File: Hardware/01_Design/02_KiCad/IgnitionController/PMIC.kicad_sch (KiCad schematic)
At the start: 0 parts

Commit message: PMIC HW implementation
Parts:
- added 8.2K1: R, symbol Device:R
- added C1: 100nF, symbol Device:C
- added C13, C3, C4, C5: 100n, Capacitor_SMD:C_0805_2012Metric_Pad1.18x1.45mm_HandSolder, symbol Device:C
- added C2: 100n, symbol Device:C
- added Q1: SS8050, Package_TO_SOT_SMD:SOT-563, symbol Transistor_BJT:SS8050
- added Q2, Q3: DMP6050SSD, Package_SO:SOIC-8_3.9x4.9mm_P1.27mm, symbol Transistor_FET:DMP6050SSD
- added R15, R5, R6, R7: 475R, Resistor_SMD:R_0805_2012Metric_Pad1.20x1.40mm_HandSolder, symbol Device:R
- added R16, R17, R18, R19: 0R, Resistor_SMD:R_0805_2012Metric_Pad1.20x1.40mm_HandSolder, symbol Device:R
- added R20, R21, R22: 8.2K, Resistor_SMD:R_0805_2012Metric_Pad1.20x1.40mm_HandSolder, symbol Device:R
- added R24, R26, R30, R32: 30K, Resistor_SMD:R_0805_2012Metric_Pad1.20x1.40mm_HandSolder, symbol Device:R
- added R25, R27, R29, R31, R33, R35, R36, R37, R38: 10K, Resistor_SMD:R_0805_2012Metric_Pad1.20x1.40mm_HandSolder, symbol Device:R
- added R28: 10k, Resistor_SMD:R_0805_2012Metric_Pad1.20x1.40mm_HandSolder, symbol Device:R
- added R34: 43k, Resistor_SMD:R_0805_2012Metric_Pad1.20x1.40mm_HandSolder, symbol Device:R
- added TP1: PMIC_CLK, TestPoint:TestPoint_Plated_Hole_D3.0mm, symbol Connector:TestPoint
- added TP2: SPI_CS, TestPoint:TestPoint_Plated_Hole_D3.0mm, symbol Connector:TestPoint
- added TP3: SPI_MOSI, TestPoint:TestPoint_Plated_Hole_D3.0mm, symbol Connector:TestPoint
- added TP4: SPI_MISO, TestPoint:TestPoint_Plated_Hole_D3.0mm, symbol Connector:TestPoint
- added TP5: SPI_SCK, TestPoint:TestPoint_Plated_Hole_D3.0mm, symbol Connector:TestPoint
- added TP6: KL30_ADC, TestPoint:TestPoint_Plated_Hole_D3.0mm, symbol Connector:TestPoint
- added TP7: KL15_ADC, TestPoint:TestPoint_Plated_Hole_D3.0mm, symbol Connector:TestPoint
- added TP8: VSEN_ADC, TestPoint:TestPoint_Plated_Hole_D3.0mm, symbol Connector:TestPoint
- added TP9: VMCU_ADC, TestPoint:TestPoint_Plated_Hole_D3.0mm, symbol Connector:TestPoint
- added U1: ATmega328PB-A, Package_QFP:TQFP-32_7x7mm_P0.8mm, symbol MCU_Microchip_ATmega:ATmega328PB-A
- added U10, U11: TLV2372, Package_SO:SOIC-8_5.3x6.2mm_P1.27mm, symbol Amplifier_Operational:TLV2372
- added U2, U5, U6, U7: 4N35, Package_DIP:DIP-6_W7.62mm, symbol Isolator:4N35
- added U8: TXS0104EPW, Package_SO:TSSOP-14_4.4x5mm_P0.65mm, symbol Logic_LevelTranslator:TXS0104EPW
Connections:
- new net: C3.1, R22.2, TP8.1, U11.1, U11.2 (-)
- new net: C2.1, R21.2, TP7.1, U10.6 (-), U10.7
- new net: Q3.2 (G1), U6.4
- new net: Q1.2 (E), R33.1, U8.8 (OE)
- new net: R18.1, U6.6
- new net: R30.2, R31.1, U11.5 (+)
- new net: 8.2K1.2, C4.1, TP9.1, U11.6 (-), U11.7
- new net: Q2.4 (G2), U5.4
- new net: C13.2, U1.20 (AREF)
- new net: R20.1, U1.23 (PC0)
- new net: C1.1, R20.2, TP6.1, U10.1, U10.2 (-)
- new net: R16.1, U2.6
- new net: TP2.1, U1.14 (PB2), U8.13 (B1)
- new net: Q3.4 (G2), U7.4
- new net: R7.2, U6.1
- new net: R28.2, TP1.1, U1.12 (PB0)
- new net: TP3.1, U1.15 (PB3), U8.12 (B2)
- new net: TP4.1, U1.16 (PB4), U8.11 (B3)
- new net: TP5.1, U1.17 (PB5), U8.10 (B4)
- new net: R21.1, U1.24 (PC1)
- new net: R22.1, U1.25 (PC2)
- new net: 8.2K1.1, U1.26 (PC3)
- new net: R5.1, U1.27 (PC4)
- new net: R6.1, U1.28 (PC5)
- new net: R7.1, U1.29 (~{RESET}/PC6)
- new net: R15.1, U1.30 (PD0)
- new net: Q2.2 (G1), U2.4
- new net: R19.1, U7.6
- new net: R29.1, R32.2, U11.3 (+)
- new net: R6.2, U5.1
- new net: R17.1, U5.6
- new net: R24.2, R25.1, U10.3 (+)
- new net: Q1.1 (B), R34.1
- new net: R15.2, U7.1
- new net: R5.2, U2.1
- new net: R26.2, R27.1, U10.5 (+)
- new net +BATT: Q2.1 (S1), Q2.3 (S2), R24.1, U2.5, U5.5
- new net GND: C1.2, C13.1, C2.2, C3.2, C4.2, C5.1, R16.2, R17.2, R18.2, R19.2, R25.2, R27.2, R28.1, R29.2, R31.2, R33.2, R35.2, R36.2, R37.2, R38.2, U1.21 (GND), U1.5 (GND), U10.4 (V-), U11.4 (V-), U2.2, U5.2, U6.2, U7.2, U8.7 (GND)
- new net KL15: R26.1
- new net KL15_OUT: Q2.5 (D2), Q2.6 (D2), R37.1
- new net KL30_OUT: Q2.7 (D1), Q2.8 (D1), R38.1
- new net MCU_SPI_CS: U8.2 (A1)
- new net MCU_SPI_MISO: U8.4 (A3)
- new net MCU_SPI_MOSI: U8.3 (A2)
- new net MCU_SPI_SCK: U8.5 (A4)
- new net OE_PIN: R34.2
- new net VMCU: Q1.3 (C), Q3.3 (S2), R30.1, U7.5, U8.1 (V_{CCA})
- new net VMCU_OUT: Q3.5 (D2), Q3.6 (D2), R35.1
- new net VPMIC: C5.2, U1.18 (AVCC), U1.4 (VCC), U10.8 (V+), U11.8 (V+), U8.14 (V_{CCB})
- new net VSEN: Q3.1 (S1), R32.1, U6.5
- new net VSENS_OUT: Q3.7 (D1), Q3.8 (D1), R36.1
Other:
- note added: "Cutoff frequency 200Hz"
- note added: "KL15"
- note added: "KL30"
- note added: "SPI Lines"
- note added: "VMCU"
- note added: "VSENS"

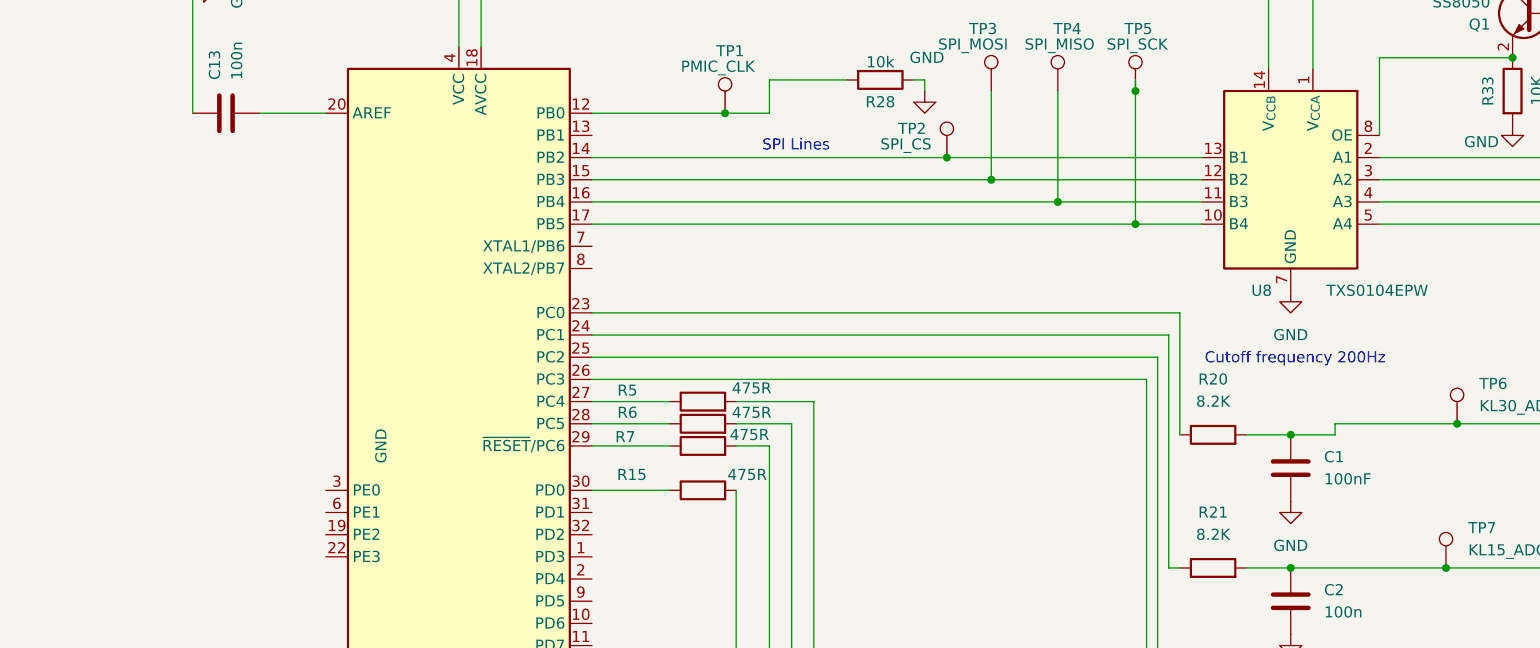
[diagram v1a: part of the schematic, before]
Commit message: Updated sch and footprints
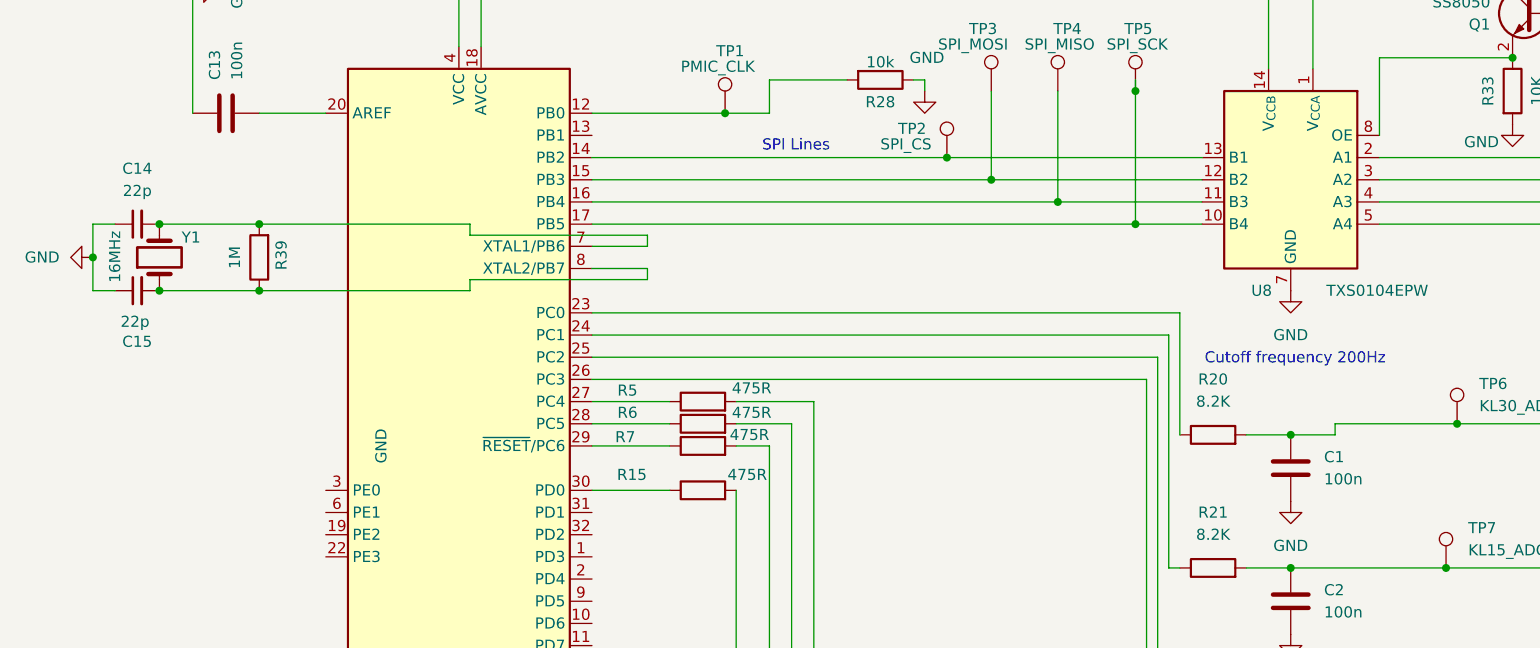
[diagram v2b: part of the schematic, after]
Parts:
- added C14, C15: 22p, symbol Device:C_Small
- added R39: 1M, Resistor_SMD:R_0805_2012Metric_Pad1.20x1.40mm_HandSolder, symbol Device:R
- added Y1: 16MHz, symbol Device:Crystal
- 8.2K1: footprint (none) -> Resistor_SMD:R_0815_2038Metric_Pad1.20x4.05mm_HandSolder
- C1: value 100nF -> 100n; footprint (none) -> Capacitor_SMD:C_0805_2012Metric_Pad1.18x1.45mm_HandSolder
- C2: footprint (none) -> Capacitor_SMD:C_0805_2012Metric_Pad1.18x1.45mm_HandSolder
- Q1: footprint Package_TO_SOT_SMD:SOT-563 -> Package_TO_SOT_SMD:TSOT-23_HandSoldering
- U2, U5, U6, U7: footprint Package_DIP:DIP-6_W7.62mm -> Library:SMD-6_7
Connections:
- net GND: now also C14.1, C15.1
- net at U1.7 (XTAL1/PB6): now also C14.2, R39.2, Y1.2
- net at U1.8 (XTAL2/PB7): now also C15.2, R39.1, Y1.1

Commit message: Peripherals Update
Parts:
- R23: renamed from 8.2K1; value R -> 8.2K1
- R24, R26, R30, R32: value 30K -> 69K8
- R25, R27, R29, R31: value 10K -> 12K1
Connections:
- net at R22.2, TP8.1, U11.1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: no longer C3.1
- net at R21.2, TP7.1, U10.6 (-)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: no longer C2.1
- net at R23.2, TP9.1, U11.6 (-)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: no longer C4.1
- net ADC_VBAT: now reaches R20.1, U1.23 (PC0)
- net ADC_VBAT: now also C1.1
- net at R20.2, TP6.1, U10.1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: no longer C1.1
- net ADC_VIGNTION: now reaches R21.1, U1.24 (PC1)
- net ADC_VIGNTION: now also C2.1
- net ADC_VSENS: now reaches R22.1, U1.25 (PC2)
- net ADC_VSENS: now also C3.1
- net ADC_VMCU: now reaches R23.1, U1.26 (PC3)
- net ADC_VMCU: now also C4.1
- net at U1.29 (~{RESET}/PC6): no longer R7.1
- net at U1.30 (PD0): now also R7.1; no longer R15.1
- net at U1.31 (PD1): now also R15.1
- net VSENS_OUT renamed VSEN_OUT
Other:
- moved on the sheet: R15, R20, R21, R22, R23, R7

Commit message: Updates to HW Layout
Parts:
- C14, C15: footprint (none) -> Capacitor_SMD:C_0805_2012Metric_Pad1.18x1.45mm_HandSolder
- TP1, TP2, TP3, TP4, TP5, TP6, TP7, TP8, TP9: footprint TestPoint:TestPoint_Plated_Hole_D3.0mm -> TestPoint:TestPoint_Pad_1.0x1.0mm
- U2, U5, U6, U7: footprint Library:SMD-6_7 -> 4N35S:4N35S
- Y1: footprint (none) -> Crystal:Crystal_HC52-8mm_Horizontal
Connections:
- net PMIC_SPI_MOSI: now reaches TP3.1, U1.15 (PB3), U8.12 (B2)
- net PMIC_SPI_MISO: now reaches TP4.1, U1.16 (PB4), U8.11 (B3)
- net PMIC_SPI_SCK: now reaches TP5.1, U1.17 (PB5), U8.10 (B4)
- net PMIC_RESET: now reaches U1.29 (~{RESET}/PC6)
- no-connect marks 0 -> 11

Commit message: Initial routing of Power supply
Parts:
- C1, C13, C14, C15, C2, C3, C4, C5: footprint Capacitor_SMD:C_0805_2012Metric_Pad1.18x1.45mm_HandSolder -> Capacitor_SMD:C_0603_1608Metric_Pad1.08x0.95mm_HandSolder
- R15, R16, R17, R18, R19, R20, R21, R22, R24, R25, R26, R27, R28, R29, R30, R31, R32, R33, R34, R35, R36, R37, R38, R39, R5, R6, R7: footprint Resistor_SMD:R_0805_2012Metric_Pad1.20x1.40mm_HandSolder -> Resistor_SMD:R_0603_1608Metric_Pad0.98x0.95mm_HandSolder
- R23: footprint Resistor_SMD:R_0815_2038Metric_Pad1.20x4.05mm_HandSolder -> Resistor_SMD:R_0603_1608Metric_Pad0.98x0.95mm_HandSolder
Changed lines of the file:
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@@
 			)
 		)
-		(property "Footprint" "Capacitor_SMD:C_0805_2012Metric_Pad1.18x1.45mm_HandSolder"
+		(property "Footprint" "Capacitor_SMD:C_0603_1608Metric_Pad1.08x0.95mm_HandSolder"
 			(at 157.1752 129.54 0)
 			(effects
@@
 			)
 		)
-		(property "Footprint" "Capacitor_SMD:C_0805_2012Metric_Pad1.18x1.45mm_HandSolder"
+		(property "Footprint" "Capacitor_SMD:C_0603_1608Metric_Pad1.08x0.95mm_HandSolder"
 			(at 157.1752 113.03 0)
 			(effects
@@
 			)
 		)
-		(property "Footprint" "Resistor_SMD:R_0805_2012Metric_Pad1.20x1.40mm_HandSolder"
+		(property "Footprint" "Resistor_SMD:R_0603_1608Metric_Pad0.98x0.95mm_HandSolder"
 			(at 179.832 50.8 90)
 			(effects
@@
 			)
 		)
-		(property "Footprint" "Resistor_SMD:R_0805_2012Metric_Pad1.20x1.40mm_HandSolder"
+		(property "Footprint" "Resistor_SMD:R_0603_1608Metric_Pad0.98x0.95mm_HandSolder"
 			(at 50.292 163.83 90)
 			(effects
@@
 			)
 		)
-		(property "Footprint" "Capacitor_SMD:C_0805_2012Metric_Pad1.18x1.45mm_HandSolder"
+		(property "Footprint" "Capacitor_SMD:C_0603_1608Metric_Pad1.08x0.95mm_HandSolder"
 			(at 24.13 66.04 0)
 			(effects
@@
 			)
 		)
-		(property "Footprint" "Capacitor_SMD:C_0805_2012Metric_Pad1.18x1.45mm_HandSolder"
+		(property "Footprint" "Capacitor_SMD:C_0603_1608Metric_Pad1.08x0.95mm_HandSolder"
 			(at 38.1 52.3748 0)
 			(effects
@@
 			)
 		)
-		(property "Footprint" "Resistor_SMD:R_0805_2012Metric_Pad1.20x1.40mm_HandSolder"
+		(property "Footprint" "Resistor_SMD:R_0603_1608Metric_Pad0.98x0.95mm_HandSolder"
 			(at 166.37 90.678 90)
 			(effects
@@
 			)
 		)
-		(property "Footprint" "Resistor_SMD:R_0805_2012Metric_Pad1.20x1.40mm_HandSolder"
+		(property "Footprint" "Resistor_SMD:R_0603_1608Metric_Pad0.98x0.95mm_HandSolder"
 			(at 85.852 163.83 90)
 			(effects
@@
 			)
 		)
-		(property "Footprint" "Resistor_SMD:R_0805_2012Metric_Pad1.20x1.40mm_HandSolder"
+		(property "Footprint" "Resistor_SMD:R_0603_1608Metric_Pad0.98x0.95mm_HandSolder"
 			(at 16.002 189.23 90)
 			(effects
@@
 			)
 		)
-		(property "Footprint" "Resistor_SMD:R_0805_2012Metric_Pad1.20x1.40mm_HandSolder"
+		(property "Footprint" "Resistor_SMD:R_0603_1608Metric_Pad0.98x0.95mm_HandSolder"
 			(at 32.512 163.83 90)
 			(effects
@@
 			)
 		)
-		(property "Footprint" "Resistor_SMD:R_0815_2038Metric_Pad1.20x4.05mm_HandSolder"
+		(property "Footprint" "Resistor_SMD:R_0603_1608Metric_Pad0.98x0.95mm_HandSolder"
 			(at 162.56 142.748 90)
 			(effects
@@
 			)
 		)
-		(property "Footprint" "Capacitor_SMD:C_0805_2012Metric_Pad1.18x1.45mm_HandSolder"
+		(property "Footprint" "Capacitor_SMD:C_0603_1608Metric_Pad1.08x0.95mm_HandSolder"
 			(at 157.1752 97.79 0)
 			(effects
@@
 			)
 		)
-		(property "Footprint" "Resistor_SMD:R_0805_2012Metric_Pad1.20x1.40mm_HandSolder"
+		(property "Footprint" "Resistor_SMD:R_0603_1608Metric_Pad0.98x0.95mm_HandSolder"
 			(at 247.142 140.97 90)
 			(effects
@@
 			)
 		)
-		(property "Footprint" "Resistor_SMD:R_0805_2012Metric_Pad1.20x1.40mm_HandSolder"
+		(property "Footprint" "Resistor_SMD:R_0603_1608Metric_Pad0.98x0.95mm_HandSolder"
 			(at 88.9 98.298 90)
 			(effects
@@
 			)
 		)
-		(property "Footprint" "Resistor_SMD:R_0805_2012Metric_Pad1.20x1.40mm_HandSolder"
+		(property "Footprint" "Resistor_SMD:R_0603_1608Metric_Pad0.98x0.95mm_HandSolder"
 			(at 247.142 151.13 90)
 			(effects
@@
 			)
 		)
-		(property "Footprint" "Resistor_SMD:R_0805_2012Metric_Pad1.20x1.40mm_HandSolder"
+		(property "Footprint" "Resistor_SMD:R_0603_1608Metric_Pad0.98x0.95mm_HandSolder"
 			(at 243.332 92.71 90)
 			(effects
@@
 			)
 		)
-		(property "Footprint" "Capacitor_SMD:C_0805_2012Metric_Pad1.18x1.45mm_HandSolder"
+		(property "Footprint" "Capacitor_SMD:C_0603_1608Metric_Pad1.08x0.95mm_HandSolder"
 			(at 157.1752 148.59 0)
 			(effects
@@
 			)
 		)
-		(property "Footprint" "Resistor_SMD:R_0805_2012Metric_Pad1.20x1.40mm_HandSolder"
+		(property "Footprint" "Resistor_SMD:R_0603_1608Metric_Pad0.98x0.95mm_HandSolder"
 			(at 70.612 189.23 90)
 			(effects
@@
 			)
 		)
-		(property "Footprint" "Resistor_SMD:R_0805_2012Metric_Pad1.20x1.40mm_HandSolder"
+		(property "Footprint" "Resistor_SMD:R_0603_1608Metric_Pad0.98x0.95mm_HandSolder"
 			(at 196.85 43.688 90)
 			(effects
@@
 			)
 		)
-		(property "Footprint" "Resistor_SMD:R_0805_2012Metric_Pad1.20x1.40mm_HandSolder"
+		(property "Footprint" "Resistor_SMD:R_0603_1608Metric_Pad0.98x0.95mm_HandSolder"
 			(at 88.9 100.838 90)
 			(effects
@@
 			)
 		)
-		(property "Footprint" "Resistor_SMD:R_0805_2012Metric_Pad1.20x1.40mm_HandSolder"
+		(property "Footprint" "Resistor_SMD:R_0603_1608Metric_Pad0.98x0.95mm_HandSolder"
 			(at 35.052 189.23 90)
 			(effects
@@
 			)
 		)
-		(property "Footprint" "Resistor_SMD:R_0805_2012Metric_Pad1.20x1.40mm_HandSolder"
+		(property "Footprint" "Resistor_SMD:R_0603_1608Metric_Pad0.98x0.95mm_HandSolder"
 			(at 88.9 88.138 90)
 			(effects
@@
 			)
 		)
-		(property "Footprint" "Resistor_SMD:R_0805_2012Metric_Pad1.20x1.40mm_HandSolder"
+		(property "Footprint" "Resistor_SMD:R_0603_1608Metric_Pad0.98x0.95mm_HandSolder"
 			(at 248.412 101.6 90)
 			(effects
@@
 			)
 		)
-		(property "Footprint" "Capacitor_SMD:C_0805_2012Metric_Pad1.18x1.45mm_HandSolder"
+		(property "Footprint" "Capacitor_SMD:C_0603_1608Metric_Pad1.08x0.95mm_HandSolder"
 			(at 24.13 73.66 0)
 			(effects
@@
 			)
 		)
-		(property "Footprint" "Resistor_SMD:R_0805_2012Metric_Pad1.20x1.40mm_HandSolder"
+		(property "Footprint" "Resistor_SMD:R_0603_1608Metric_Pad0.98x0.95mm_HandSolder"
 			(at 162.56 123.698 90)
 			(effects
@@
 			)
 		)
-		(property "Footprint" "Resistor_SMD:R_0805_2012Metric_Pad1.20x1.40mm_HandSolder"
+		(property "Footprint" "Resistor_SMD:R_0603_1608Metric_Pad0.98x0.95mm_HandSolder"
 			(at 248.412 111.76 90)
 			(effects
@@
 			)
 		)
-		(property "Footprint" "Resistor_SMD:R_0805_2012Metric_Pad1.20x1.40mm_HandSolder"
+		(property "Footprint" "Resistor_SMD:R_0603_1608Metric_Pad0.98x0.95mm_HandSolder"
 			(at 242.062 132.08 90)
 			(effects
@@
 			)
 		)
-		(property "Footprint" "Resistor_SMD:R_0805_2012Metric_Pad1.20x1.40mm_HandSolder"
+		(property "Footprint" "Resistor_SMD:R_0603_1608Metric_Pad0.98x0.95mm_HandSolder"
 			(at 109.22 47.752 90)
 			(effects
@@
 			)
 		)
-		(property "Footprint" "Resistor_SMD:R_0805_2012Metric_Pad1.20x1.40mm_HandSolder"
+		(property "Footprint" "Resistor_SMD:R_0603_1608Metric_Pad0.98x0.95mm_HandSolder"
 			(at 243.332 82.55 90)
 			(effects
@@
 			)
 		)
-		(property "Footprint" "Resistor_SMD:R_0805_2012Metric_Pad1.20x1.40mm_HandSolder"
+		(property "Footprint" "Resistor_SMD:R_0603_1608Metric_Pad0.98x0.95mm_HandSolder"
 			(at 242.062 121.92 90)
 			(effects
@@
 			)
 		)
-		(property "Footprint" "Resistor_SMD:R_0805_2012Metric_Pad1.20x1.40mm_HandSolder"
+		(property "Footprint" "Resistor_SMD:R_0603_1608Metric_Pad0.98x0.95mm_HandSolder"
 			(at 52.832 189.23 90)
 			(effects
@@
 			)
 		)
-		(property "Footprint" "Resistor_SMD:R_0805_2012Metric_Pad1.20x1.40mm_HandSolder"
+		(property "Footprint" "Resistor_SMD:R_0603_1608Metric_Pad0.98x0.95mm_HandSolder"
 			(at 88.9 90.678 90)
 			(effects
@@
 			)
 		)
-		(property "Footprint" "Resistor_SMD:R_0805_2012Metric_Pad1.20x1.40mm_HandSolder"
+		(property "Footprint" "Resistor_SMD:R_0603_1608Metric_Pad0.98x0.95mm_HandSolder"
 			(at 162.56 107.188 90)
 			(effects
@@
 			)
 		)
-		(property "Footprint" "Resistor_SMD:R_0805_2012Metric_Pad1.20x1.40mm_HandSolder"
+		(property "Footprint" "Resistor_SMD:R_0603_1608Metric_Pad0.98x0.95mm_HandSolder"
 			(at 39.878 69.85 90)
 			(effects
@@
 			)
 		)
-		(property "Footprint" "Resistor_SMD:R_0805_2012Metric_Pad1.20x1.40mm_HandSolder"
+		(property "Footprint" "Resistor_SMD:R_0603_1608Metric_Pad0.98x0.95mm_HandSolder"
 			(at 66.802 163.83 90)
 			(effects
@@
 			)
 		)
-		(property "Footprint" "Capacitor_SMD:C_0805_2012Metric_Pad1.18x1.45mm_HandSolder"
+		(property "Footprint" "Capacitor_SMD:C_0603_1608Metric_Pad1.08x0.95mm_HandSolder"
 			(at 69.5452 35.56 0)
 			(effects
